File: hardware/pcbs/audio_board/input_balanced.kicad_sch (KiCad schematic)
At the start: 11 parts, among them J1 NC3FAH1, U3 TL072

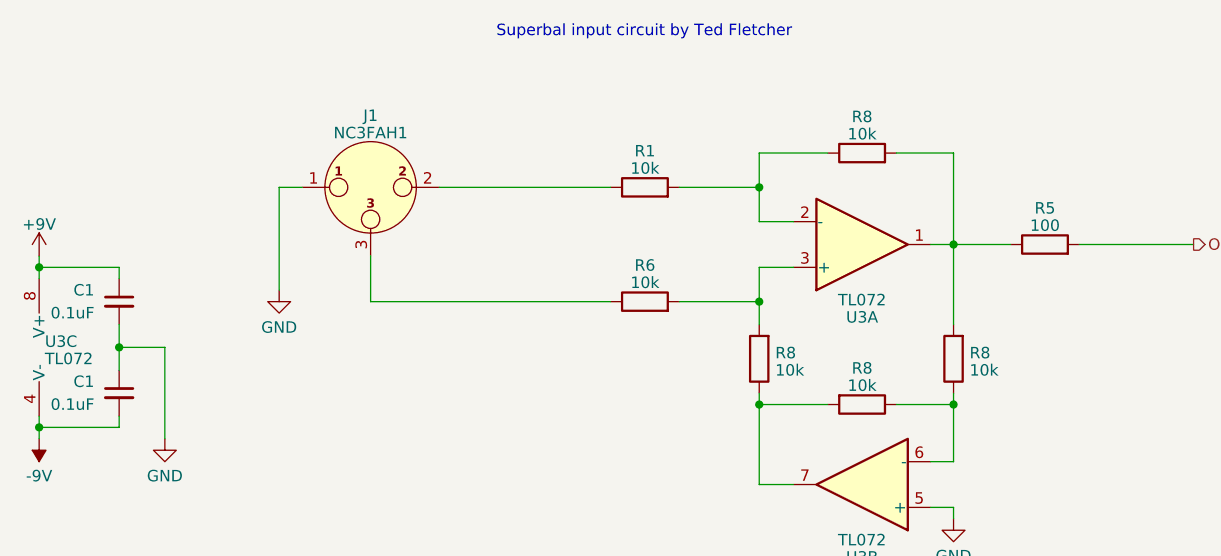
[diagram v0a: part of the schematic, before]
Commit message: Small audio board fixes and add DHAN-M module
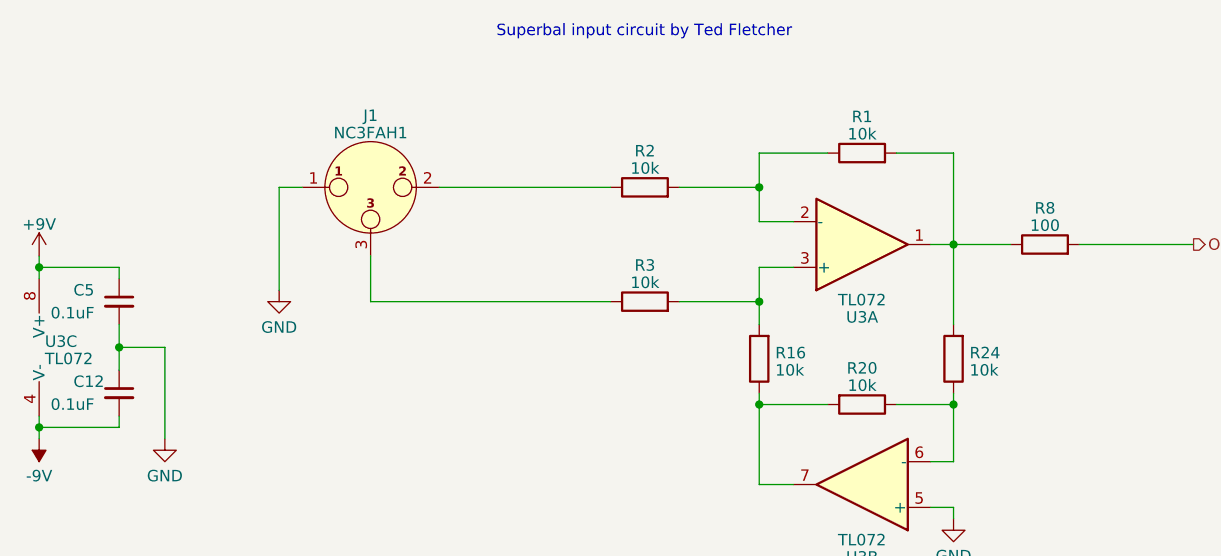
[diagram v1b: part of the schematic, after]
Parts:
- renumbered C1 to C12, C1 to C5, R8 to R1, R8 to R16, R1 to R2, R8 to R20, R8 to R24, R6 to R3, R5 to R8

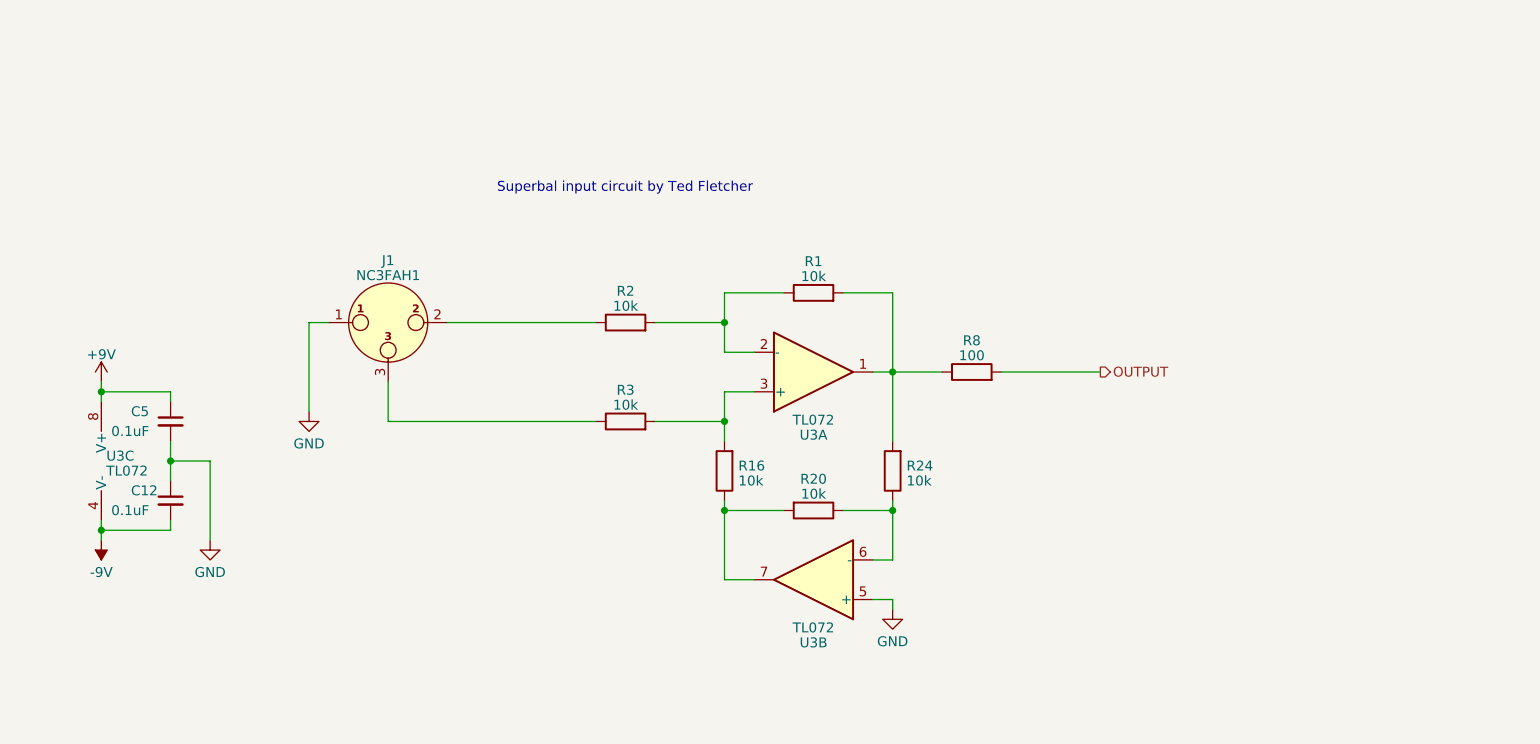
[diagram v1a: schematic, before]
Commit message: Redo layout for the audio board
* Height of the board decreased by 2cm
* Switching regulator removed
* Switched balanced audio I/O for single-rail versions
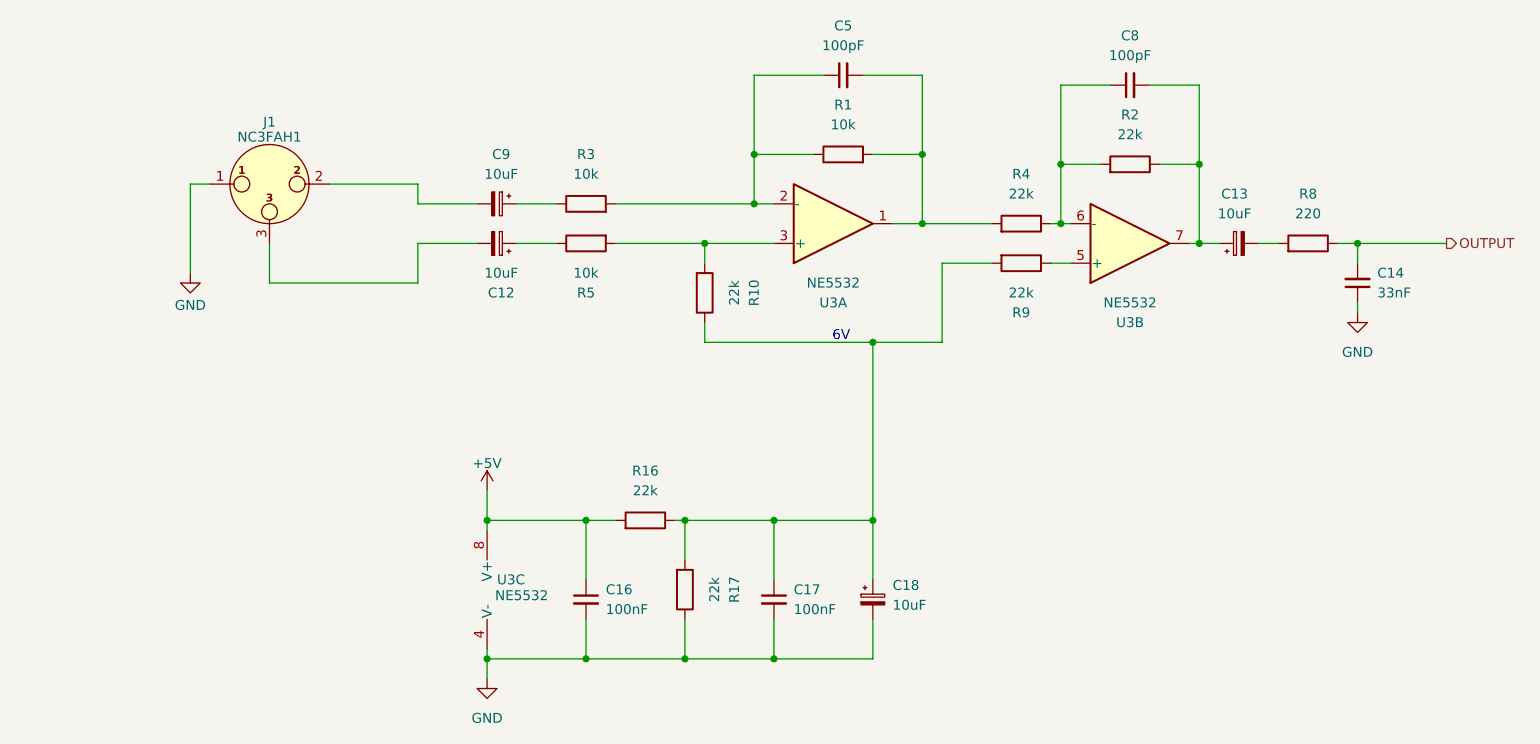
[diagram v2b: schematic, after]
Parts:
- removed C12: 0.1uF, Capacitor_SMD:C_0603_1608Metric_Pad1.08x0.95mm_HandSolder, symbol Device:C_Small
- removed R20, R24: 10k, Resistor_SMD:R_0603_1608Metric_Pad0.98x0.95mm_HandSolder, symbol Device:R
- removed U3: TL072, Package_SO:SO-8_3.9x4.9mm_P1.27mm, symbol Amplifier_Operational:TL072
- added C12, C13, C18, C9: 10uF, Capacitor_SMD:C_0805_2012Metric, symbol Device:C_Polarized_Small
- added C14: 33nF, Capacitor_SMD:C_0603_1608Metric, symbol Device:C_Small
- added C16, C17: 100nF, Capacitor_SMD:C_0603_1608Metric, symbol Device:C_Small
- added C8: 100pF, Capacitor_SMD:C_0603_1608Metric, symbol Device:C_Small
- added R10, R17, R4, R9: 22k, Resistor_SMD:R_0603_1608Metric, symbol Device:R
- added R5: 10k, Resistor_SMD:R_0603_1608Metric, symbol Device:R
- added U3: NE5532, Package_SO:SOIC-8_3.9x4.9mm_P1.27mm, symbol Amplifier_Operational:NE5532
- C5: value 0.1uF -> 100pF; footprint Capacitor_SMD:C_0603_1608Metric_Pad1.08x0.95mm_HandSolder -> Capacitor_SMD:C_0603_1608Metric; LCSC C14663 -> C14858; MPN (none) -> 885012006023
- R1, R3: footprint Resistor_SMD:R_0603_1608Metric_Pad0.98x0.95mm_HandSolder -> Resistor_SMD:R_0603_1608Metric; MPN (none) -> 560112116023
- R16, R2: value 10k -> 22k; footprint Resistor_SMD:R_0603_1608Metric_Pad0.98x0.95mm_HandSolder -> Resistor_SMD:R_0603_1608Metric; LCSC C25804 -> C31850; MPN (none) -> 560112116022
- R8: value 100 -> 220; footprint Resistor_SMD:R_0603_1608Metric_Pad0.98x0.95mm_HandSolder -> Resistor_SMD:R_0603_1608Metric; LCSC C22775 -> C23345; MPN (none) -> 560112116126
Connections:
- net +9V is gone; now on an unnamed net: C5.1
- net GND: now also C14.1, C16.2, C17.2, C18.2, R17.1, U3.4 (V-); no longer C5.2
- net OUTPUT: now also R8.1, C14.2; no longer R8.2
- net at J1.2: now also C9.2; no longer R2.1
- net at R2.2: now also C8.1, R4.1, U3.6 (-); no longer R1.1
- net at R16.1: now also C17.1, C18.1, R10.1, R17.2, R9.2
- net at R3.2: now also R1.1, U3.2 (-); no longer R16.2
- net at R1.2: now also C5.2, R4.2, U3.1; no longer R8.1
- net at J1.3: now also C12.2; no longer R3.1
- new net: C12.1, R5.1
- new net: R10.2, R5.2, U3.3 (+)
- new net: R9.1, U3.5 (+)
- new net: C13.1, C8.2, R2.1, U3.7
- new net: C13.2, R8.2
- new net: C9.1, R3.1
- new net +5V: C16.1, R16.2, U3.8 (V+)
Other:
- note added: "6V"
- note removed: "Superbal input circuit by Ted Fletcher"

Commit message: audio_board, power_board: update shop and part links
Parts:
- C12, C13, C18, C9: Part (none) -> C 10μ 16V 0805
- C14: Part (none) -> C 33nF 16V 0603
- C16, C17: Part (none) -> C 100nF 16V 0603
- C5, C8: Part (none) -> C 100pF 16V 0603
- J1: Part (none) -> NC3FAH1; Shop (none) -> https://eu.mouser.com/ProductDetail/568-NC3FAH1
- R1, R3, R5: Part (none) -> R 10kΩ 0603
- R10, R16, R17, R2, R4, R9: Part (none) -> R 22kΩ 0603
- R8: Part (none) -> R 220Ω 0603
- U3: Part (none) -> NE5532DR; Shop (none) -> https://store.comet.bg/Catalogue/Product/17010/

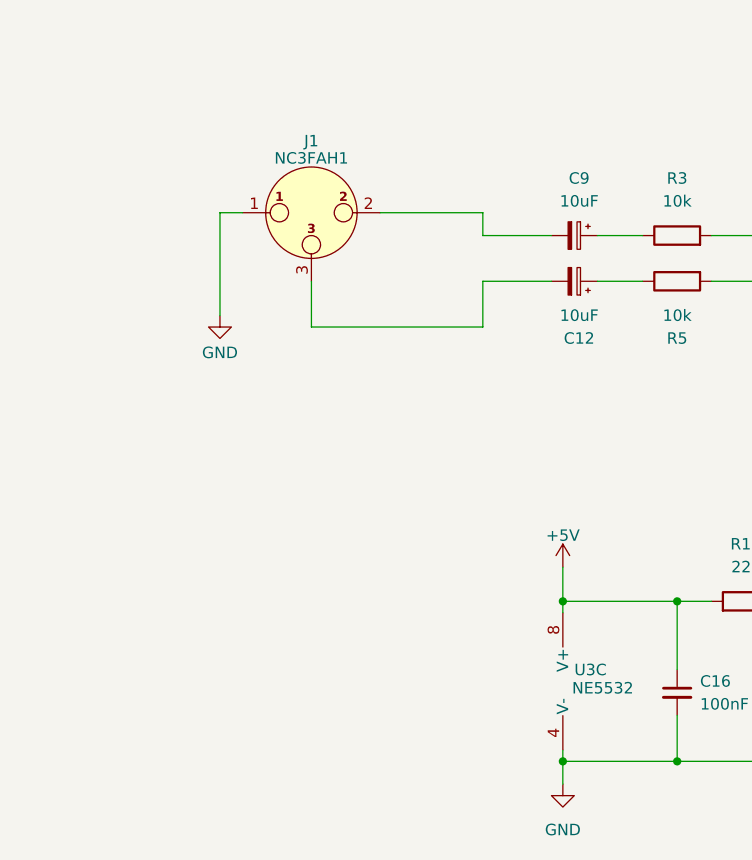
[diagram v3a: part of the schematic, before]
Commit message: Audio board revision C
* Switched the neutrik jacks to NC3FAH2 instead of FAH1 so the jacks
  with an extra ground pin fit (but the FAH1 ones also still fit)
* Added traces for optional leds (marked DNP)
* Fixed up the opamp orientation for the XLR outputs
* Moved the LCD connector to the other side of the board and switched to
  an MTA-100 connector
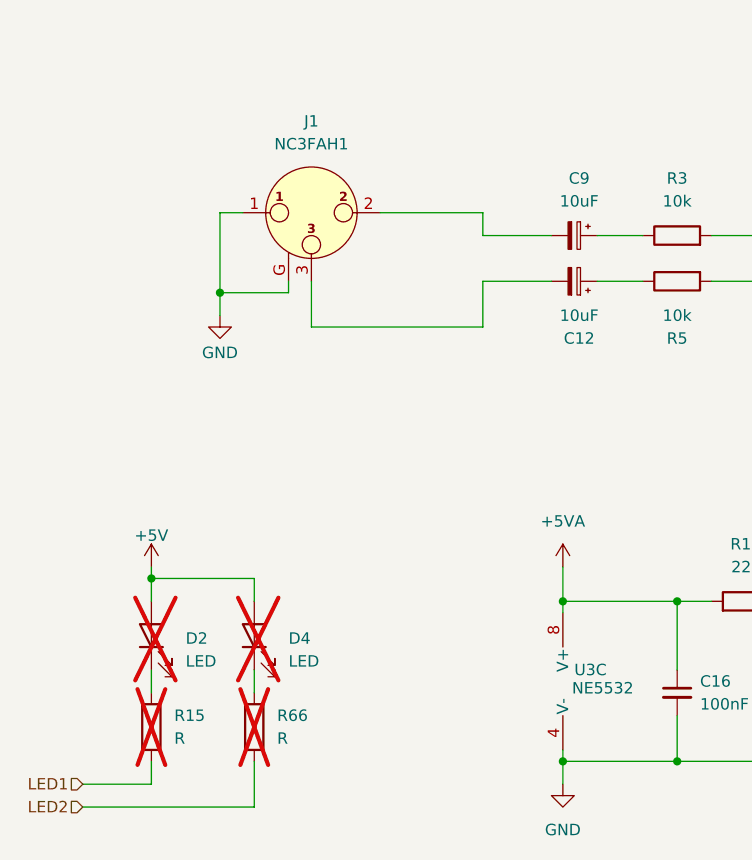
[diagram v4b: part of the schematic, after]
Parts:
- added D2, D4: LED, LED_SMD:LED_0603_1608Metric_Pad1.05x0.95mm_HandSolder, symbol Device:LED
- added R15, R66: R, Resistor_SMD:R_0603_1608Metric_Pad0.98x0.95mm_HandSolder, symbol Device:R
- C12, C13, C18, C9: Part C 10μ 16V 0805 -> (none)
- C14: Part C 33nF 16V 0603 -> (none)
- C16, C17: Part C 100nF 16V 0603 -> (none)
- C5, C8: Part C 100pF 16V 0603 -> (none)
- J1: footprint Library:Jack_XLR_Neutrik_NC3FAH1_Horizontal -> Library:Jack_XLR_Neutrik_NC3FAH2-LR-DAE_Horizontal; symbol Connector_Audio:NC3FAH1 -> Connector_Audio:NC3FAH2; Part NC3FAH1 -> (none); Shop https://eu.mouser.com/ProductDetail/568-NC3FAH1 -> (none)
- R1, R3, R5: Part R 10kΩ 0603 -> (none)
- R10, R16, R17, R2, R4, R9: Part R 22kΩ 0603 -> (none)
- R8: Part R 220Ω 0603 -> (none)
- U3: Part NE5532DR -> (none); Shop https://store.comet.bg/Catalogue/Product/17010/ -> (none)
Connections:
- net +5V: now also D2.2 (A), D4.2 (A); no longer C16.1, R16.2, U3.8 (V+)
- net GND: now also J1.G
- new net: D2.1 (K), R15.1
- new net: D4.1 (K), R66.1
- new net +5VA: C16.1, R16.2, U3.8 (V+)
- new net LED1: R15.2
- new net LED2: R66.2

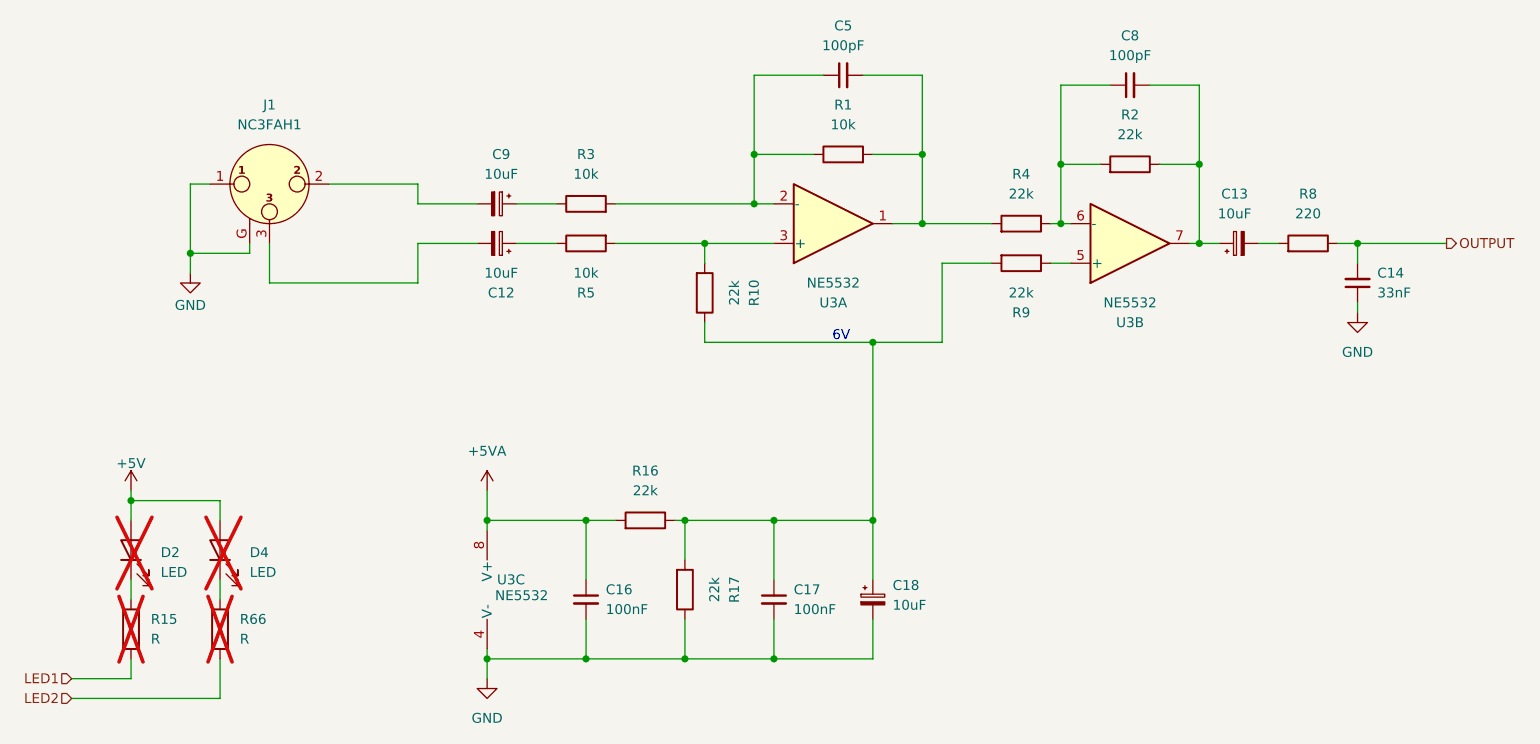
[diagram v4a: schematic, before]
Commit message: Audio board Rev. C fixes
* Switch opamp to OPA1678
* Fix filter resistor on inputs from 22 ohm to 220 ohm
* Make the board 4 layers for a better ground plane
* Implement an RC filter for the opamp 5V line
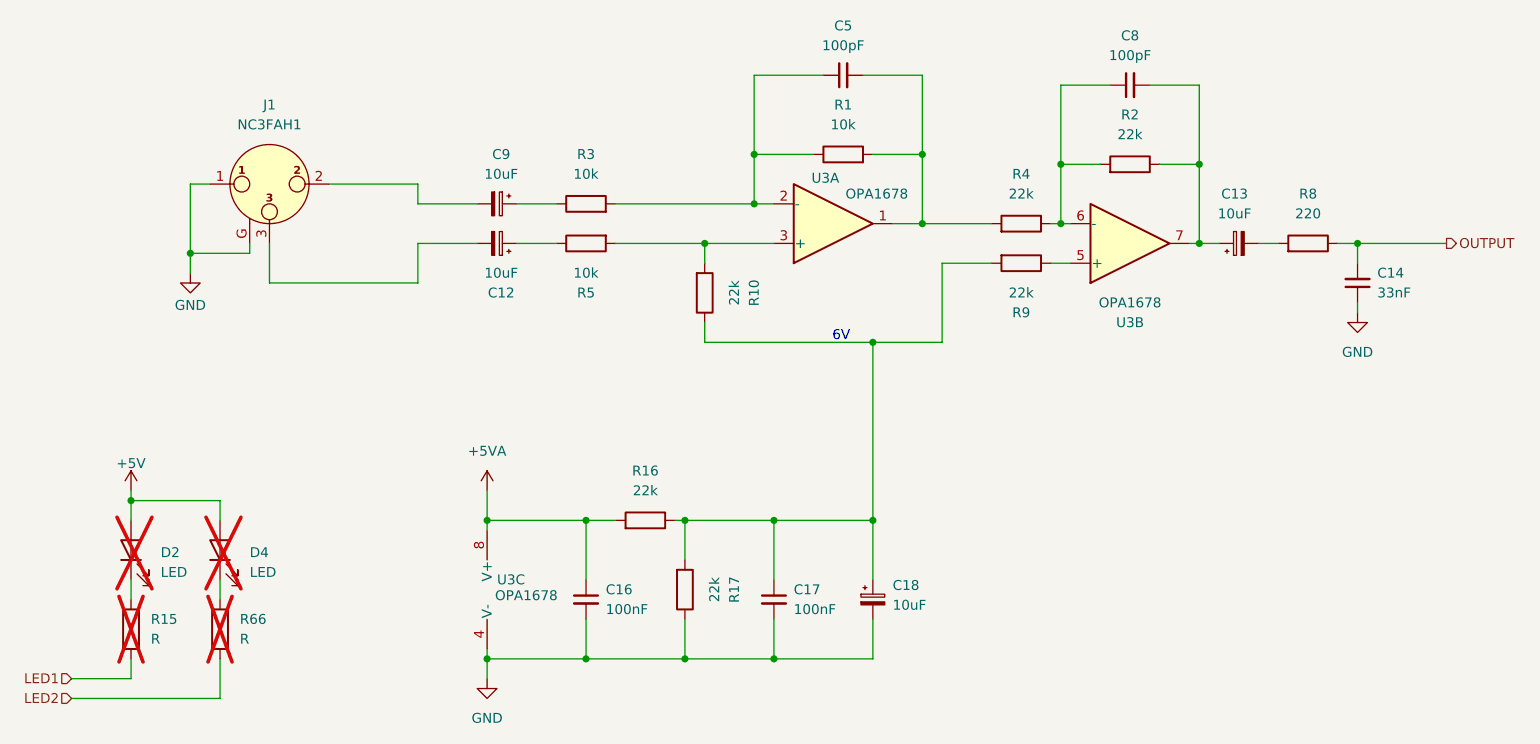
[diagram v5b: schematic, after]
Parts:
- R8: LCSC C23345 -> C22962
- U3: value NE5532 -> OPA1678; LCSC C7426 -> C192421; MPN (none) -> 595-OPA1678IDR
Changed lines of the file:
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@@
 			)
 		)
-		(property "Value" "NE5532"
+		(property "Value" "OPA1678 "
 			(at 182.88 87.63 0)
 			(effects
@@
 			)
 		)
-		(property "LCSC" "C7426"
+		(property "LCSC" "C192421"
 			(at 182.88 80.01 0)
 			(effects
@@
 			)
 		)
-		(property "MPN" ""
+		(property "MPN" "595-OPA1678IDR "
 			(at 182.88 80.01 0)
 			(effects
@@
 			)
 		)
-		(property "Value" "NE5532"
+		(property "Value" "OPA1678 "
 			(at 101.346 125.222 0)
 			(effects
@@
 			)
 		)
-		(property "LCSC" "C7426"
+		(property "LCSC" "C192421"
 			(at 102.87 124.46 0)
 			(effects
@@
 			)
 		)
-		(property "MPN" ""
+		(property "MPN" "595-OPA1678IDR "
 			(at 102.87 124.46 0)
 			(effects
@@
 			)
 		)
-		(property "LCSC" "C23345"
+		(property "LCSC" "C22962"
 			(at 205.74 80.01 0)
 			(effects
@@
 		(on_board yes)
 		(dnp no)
-		(fields_autoplaced yes)
 		(property "Reference" "U3"
-			(at 144.78 87.63 0)
-			(effects
-				(font
-					(size 1.27 1.27)
-				)
-			)
-		)
-		(property "Value" "NE5532"
-			(at 144.78 85.09 0)
+			(at 143.764 71.628 0)
+			(effects
+				(font
+					(size 1.27 1.27)
+				)
+			)
+		)
+		(property "Value" "OPA1678 "
+			(at 150.368 73.66 0)
 			(effects
 				(font
@@
 			)
 		)
-		(property "LCSC" "C7426"
+		(property "LCSC" "C192421"
 			(at 144.78 77.47 0)
 			(effects
@@
 			)
 		)
-		(property "MPN" ""
+		(property "MPN" "595-OPA1678IDR "
 			(at 144.78 77.47 0)
 			(effects
